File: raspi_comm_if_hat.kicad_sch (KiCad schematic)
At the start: 51 parts, among them J1 B04B-XA, J2 Conn_02x20_Odd_Even, J3 B04B-XA, J4 Conn_01x02, J5 Conn_01x04, J6 B04B-XA, Q1 Q_NMOS_GSD, SW1 SW_DIP_x01, SW2 SW_DIP_x02, U1 MCP25625-x-SS, U2 74AHC1G04, U3 74AHC1G04, U4 TCK106AF, U5 TCK106AF, U6 CH213K, U7 CH213K, U8 TCK106AF, U9 TCK106AF, Y1 20MHz

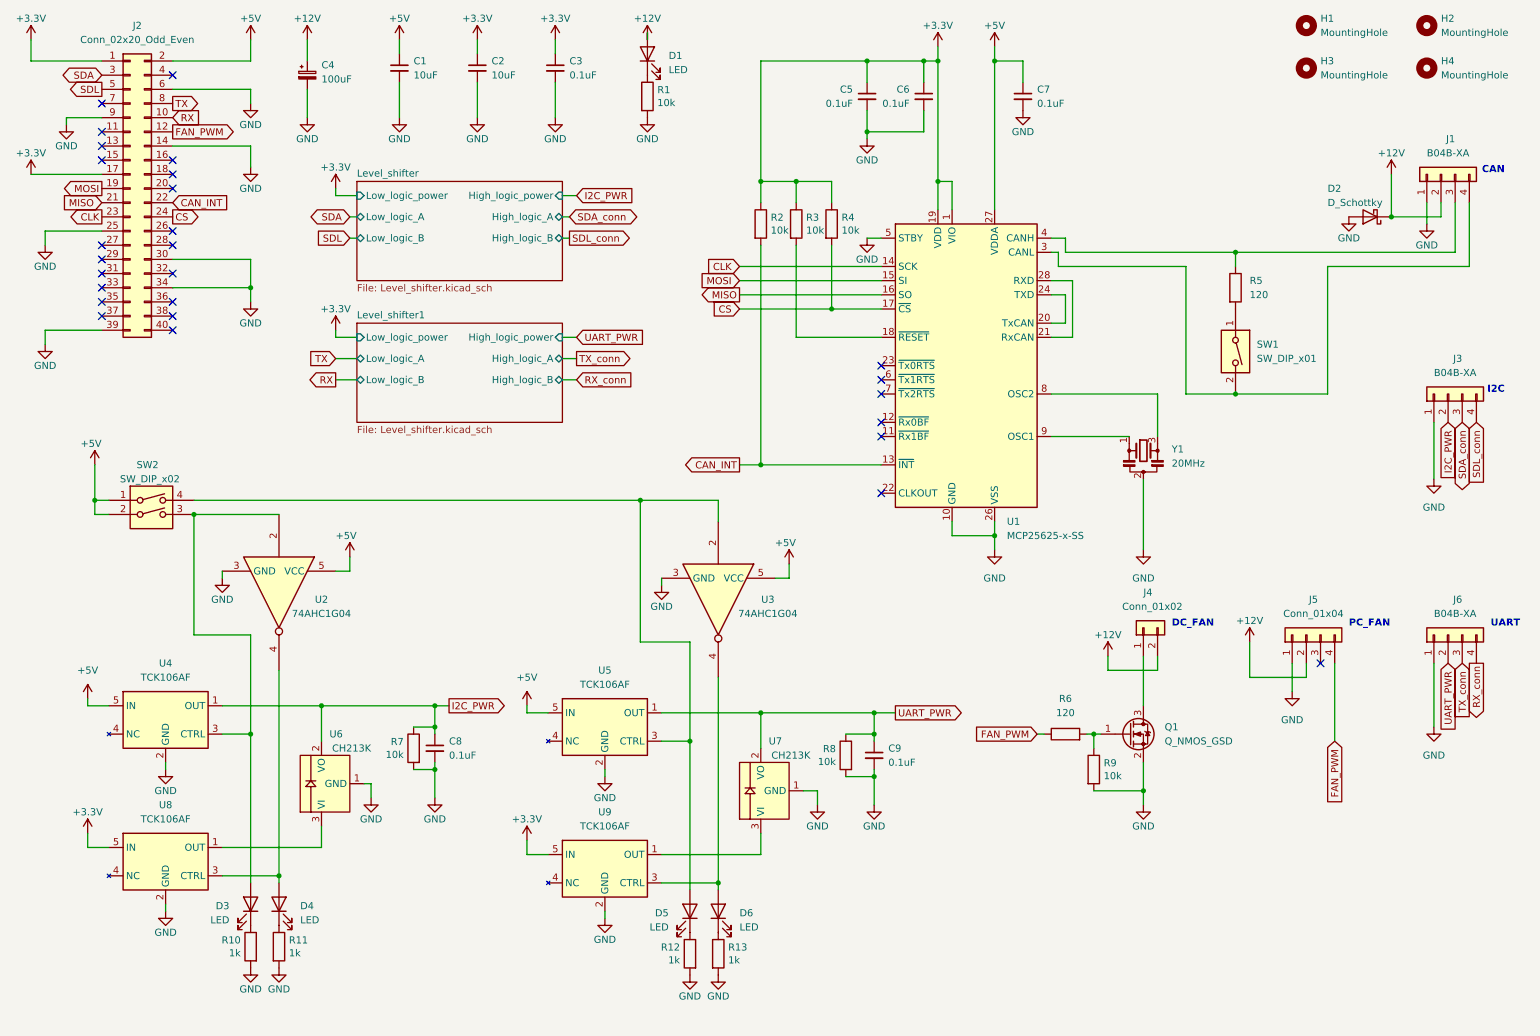
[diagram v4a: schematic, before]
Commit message: Update of data for PCBA
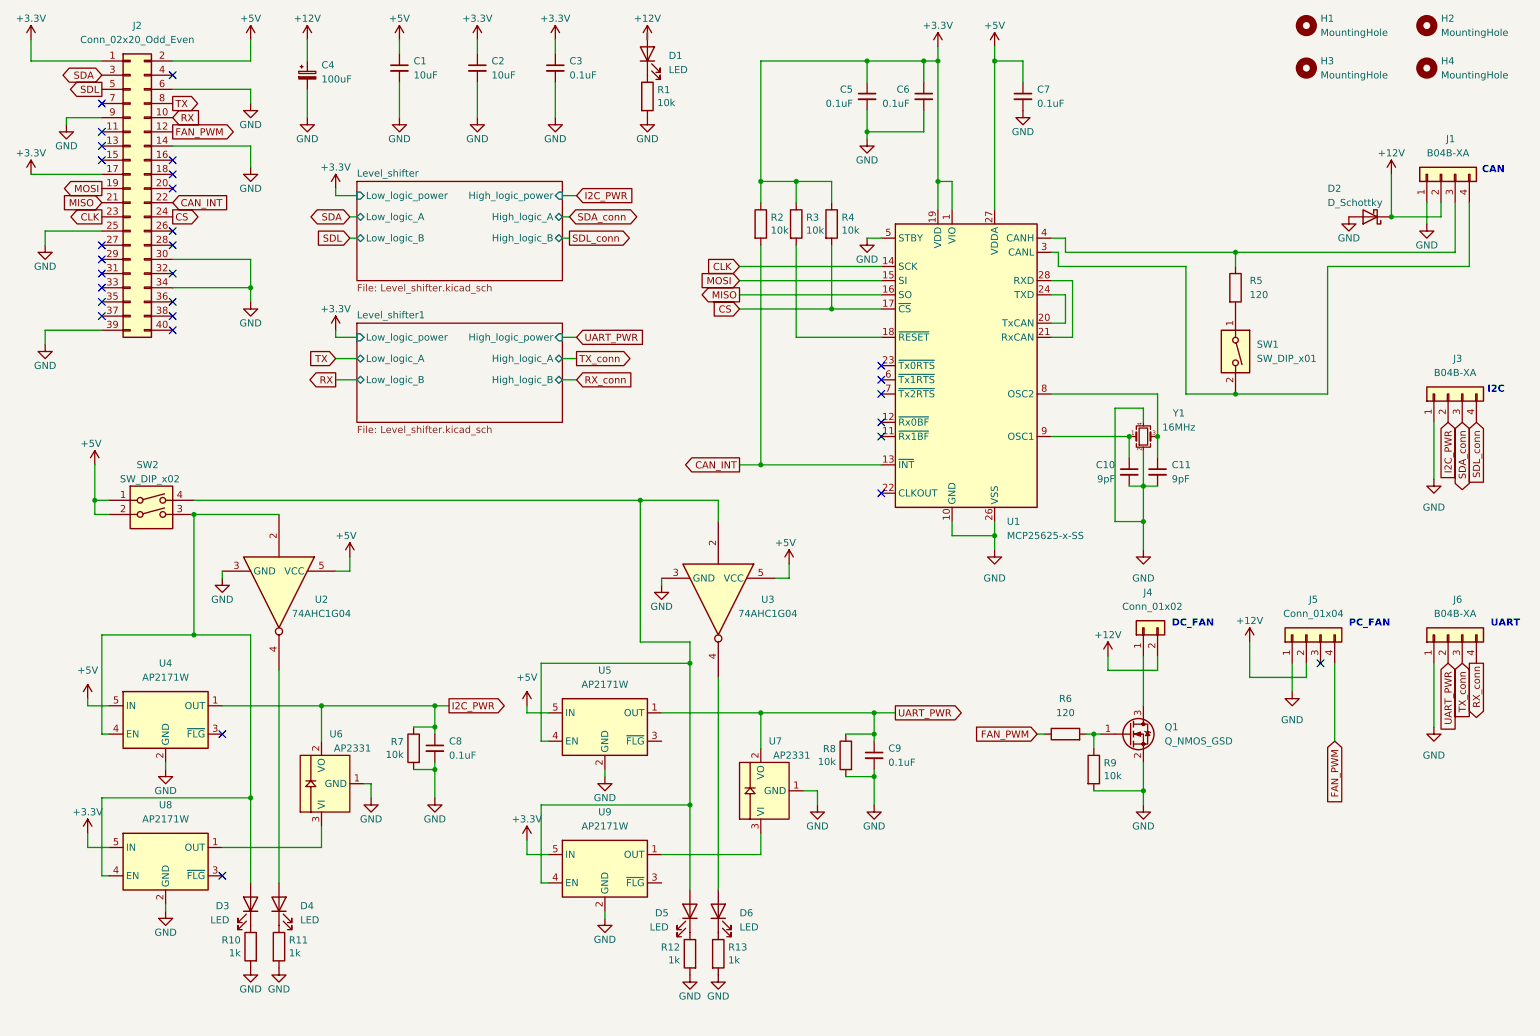
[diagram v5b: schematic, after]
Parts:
- removed U4, U5, U8, U9: TCK106AF, Package_TO_SOT_SMD:SOT-23-5, symbol RDC_generic:TCK106AF
- removed Y1: 20MHz, Crystal:Resonator_Murata_CSTLSxxxX-3Pin_W5.5mm_H3.0mm, symbol Device:Resonator_Small
- added C10, C11: 9pF, Capacitor_SMD:C_0603_1608Metric, symbol Device:C_Small
- added U4, U5, U8, U9: AP2171W, Package_TO_SOT_SMD:SOT-23-5, symbol Power_Management:AP2171W
- added Y1: 16MHz, Crystal:Crystal_SMD_3225-4Pin_3.2x2.5mm, symbol Device:Crystal_GND24_Small
- U6, U7: value CH213K -> AP2331
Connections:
- net +3.3V: now also U8.5 (IN), U9.5 (IN)
- net +5V: now also U4.5 (IN), U5.5 (IN)
- net GND: now also C10.2, C11.2, U4.2 (GND), U5.2 (GND), U8.2 (GND), U9.2 (GND), Y1.2, Y1.4
- net I2C_PWR: now also U4.1 (OUT)
- net UART_PWR: now also U5.1 (OUT)
- net at D3.2 (A), SW2.3, U2.2: now also U4.4 (EN), U8.4 (EN)
- net at D5.2 (A), SW2.4, U3.2: now also U5.4 (EN), U9.4 (EN)
- net at U7.3 (VI): now also U9.1 (OUT)
- net at U6.3 (VI): now also U8.1 (OUT)
- net at U1.8 (OSC2): now also C11.1, Y1.3
- net at U1.9 (OSC1): now also C10.1, Y1.1
- no-connect marks 27 -> 29

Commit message: Add LSCS
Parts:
- removed C4: 100uF, Capacitor_Tantalum_SMD:CP_EIA-7343-15_Kemet-W, symbol Device:C_Polarized_Small
- removed SW1: SW_DIP_x01, Button_Switch_THT:SW_DIP_SPSTx01_Slide_6.7x4.1mm_W7.62mm_P2.54mm_LowProfile, symbol Switch:SW_DIP_x01
- added C4: 10uF, Capacitor_SMD:C_0603_1608Metric, symbol Device:C_Small
- added JP1: Jumper_2_Open, Connector_PinHeader_2.54mm:PinHeader_1x02_P2.54mm_Vertical, symbol Jumper:Jumper_2_Open
- C1, C2: LCSC (none) -> C96446
- C10, C11: value 9pF -> 10pF; footprint Capacitor_SMD:C_0603_1608Metric -> Capacitor_SMD:C_0402_1005Metric; LCSC (none) -> C32949
- C3, C5, C6, C7, C8, C9: footprint Capacitor_SMD:C_0603_1608Metric -> Capacitor_SMD:C_0402_1005Metric; LCSC (none) -> C307331
- D1, D3, D4, D5, D6: LCSC (none) -> C2286
- D2: footprint Diode_SMD:Vishay_SMPA -> Diode_SMD:D_SOD-123F; LCSC (none) -> C7502712
- Q1: LCSC (none) -> C20917
- R1, R2, R3, R4, R7, R8, R9: footprint Resistor_SMD:R_0603_1608Metric_Pad0.98x0.95mm_HandSolder -> Resistor_SMD:R_0402_1005Metric; LCSC (none) -> C25744
- R10, R11, R12, R13: footprint Resistor_SMD:R_0603_1608Metric_Pad0.98x0.95mm_HandSolder -> Resistor_SMD:R_0402_1005Metric; LCSC (none) -> C11702
- R5: LCSC (none) -> C22787
- R6: footprint Resistor_SMD:R_0603_1608Metric -> Resistor_SMD:R_0402_1005Metric; LCSC (none) -> C25079
- U1: LCSC (none) -> C184944
- U2, U3: LCSC (none) -> C460486
- U4, U5, U8, U9: LCSC (none) -> C110466
- U6, U7: LCSC (none) -> C183303
- Y1: LCSC (none) -> C13738
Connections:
- net +12V: now also C4.1
- net GND: now also C4.2
- net at D3.2 (A), SW2.3, U2.2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: no longer U8.4 (EN)
- net at D5.2 (A), SW2.4, U3.2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: no longer U9.4 (EN)
- net at J1.4 (Pin_4), U1.3 (CANL): now also JP1.2 (B)
- net at D6.2 (A), U3.4: now also U9.4 (EN)
- net at R5.2: now also JP1.1 (A)
- net at D4.2 (A), U2.4: now also U8.4 (EN)
- no-connect marks 29 -> 31
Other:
- moved on the sheet: C1, C2, C3

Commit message: v0.2.0 release
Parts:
- removed J5: Conn_01x04, Connector_PinHeader_2.54mm:PinHeader_1x04_P2.54mm_Vertical, symbol Connector_Generic:Conn_01x04
- removed U4, U5, U8, U9: AP2171W, Package_TO_SOT_SMD:SOT-23-5, symbol Power_Management:AP2171W
- removed U6, U7: AP2331, Package_TO_SOT_SMD:SOT-23, symbol RDC_generic:CH213K
- added U4, U5, U6, U7: XC8110, Package_TO_SOT_SMD:SOT-23-5, symbol RDC_generic:XC8110
- J1, J3, J6: footprint Connector_JST:JST_XA_B04B-XASK-1_1x04_P2.50mm_Vertical -> Connector_JST:JST_XA_S04B-XASK-1_1x04_P2.50mm_Horizontal
- U2, U3: FT Rotation Offset (none) -> 90
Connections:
- net +3.3V: now also U5.1 (IN), U7.1 (IN)
- net +5V: now also U4.1 (IN), U6.1 (IN)
- net GND: now also U4.2 (GND), U5.2 (GND), U6.2 (GND), U7.2 (GND)
- net I2C_PWR: now also U4.5 (OUT), U5.5 (OUT)
- net UART_PWR: now also U6.5 (OUT), U7.5 (OUT)
- net at D3.2 (A), SW2.3, U2.2: now also U4.3 (CE)
- net at D5.2 (A), SW2.4, U3.2: now also U6.3 (CE)
- net at D6.2 (A), U3.4: now also U7.3 (CE)
- net at D4.2 (A), U2.4: now also U5.3 (CE)
- no-connect marks 31 -> 26
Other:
- note removed: "PC_FAN"
- moved on the sheet: J4, Q1, R6, R9
